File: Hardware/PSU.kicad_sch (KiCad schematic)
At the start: 0 parts

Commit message: started regulator circuit, EN circuit is not finished yet
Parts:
- added BT1, BT2, BT3: Battery_Cell, symbol Device:Battery_Cell
- added C14, C15, C16, C17, C18, C19: C, symbol Device:C
- added R12, R13, R14, R15: R, symbol Device:R
- added SW1: SW_SPDT, symbol Switch:SW_SPDT
- added U4: TLV74115_SOT23-5, Package_TO_SOT_SMD:SOT-23-5, symbol Custom_Regulator_Linear:TLV74115_SOT23-5
- added U5: TLV74133_SOT23-5, Package_TO_SOT_SMD:SOT-23-5, symbol Custom_Regulator_Linear:TLV74133_SOT23-5
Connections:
- new net: C18.1, R12.1, R13.2, U5.3 (EN)
- new net: C14.1, U5.1 (IN)
- new net: C16.1, U4.1 (IN)
- new net: C19.1, R14.2, R15.1, U4.3 (EN)
- new net +BATT: BT3.1 (+), SW1.2 (B)
- new net 1V5: C17.1, U4.5 (OUT)
- new net 3V3: C15.1, U5.5 (OUT)
- new net C1: BT1.1 (+), BT2.2 (-)
- new net C2: BT2.1 (+), BT3.2 (-)
- new net GND: BT1.2 (-), C14.2, C15.2, C16.2, C17.2, C18.2, C19.2, R12.2, R15.2, U4.2 (GND), U5.2 (GND)
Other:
- note added: "EN>=0.9V ACTIVE EN<=0.4V INACTIVE 3.9V/0.4V9.75V/V 3.9V/10V/V=0.39V"
- note added: "VBATT_MAX_ALKALINE=3*1.6V=4.8V VBATT_MIN_ALKALINE=3*1.1V=3.3V V_DROPOUT_MAX=540mV@150mA 3.3V+540mV≈3.9V"

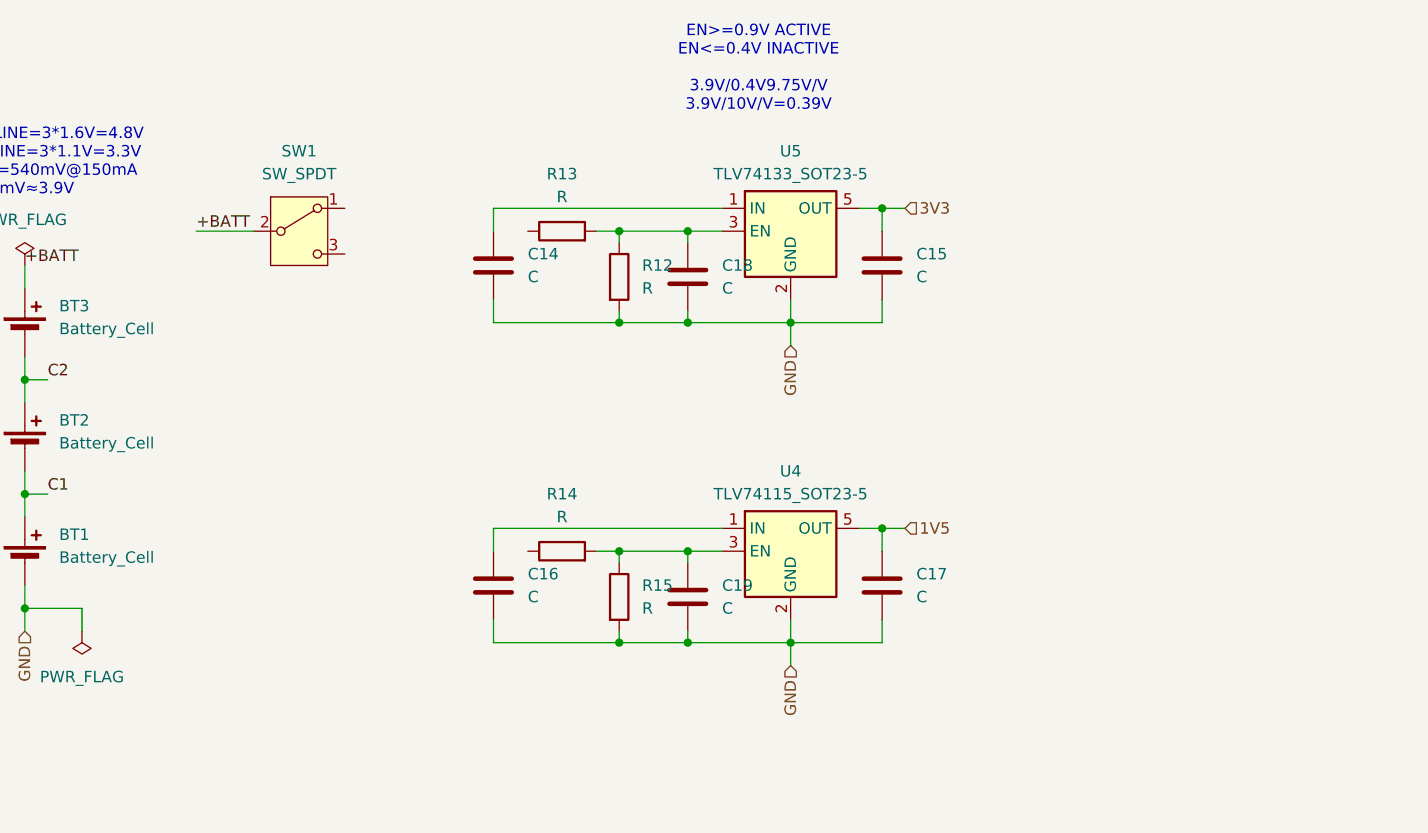
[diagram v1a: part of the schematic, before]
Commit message: Did to much for one commit BAD
- calculated values for EN divider in PSU sheet
- added power flag to switch output in PSU sheet
- connected the different sheets in the Root page
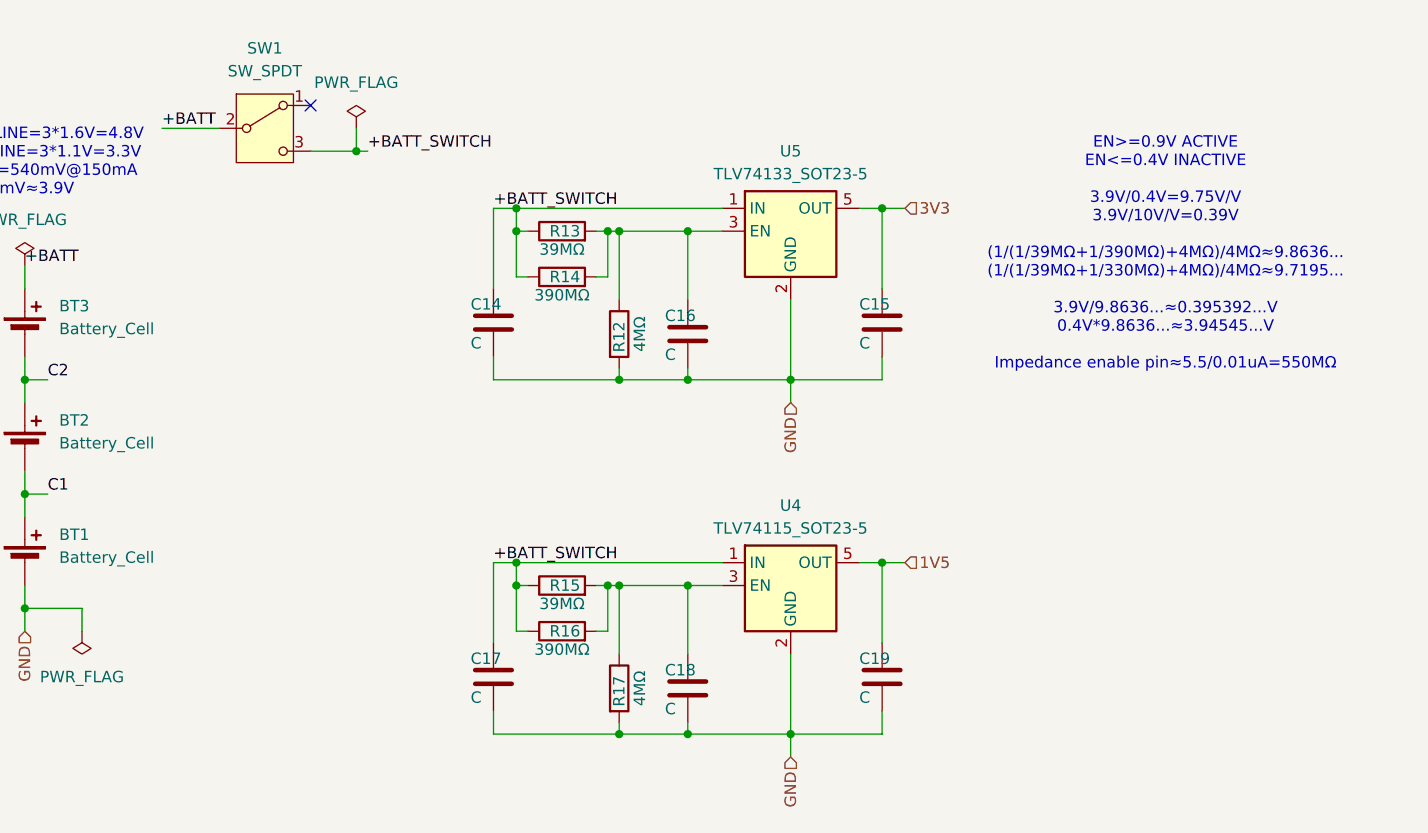
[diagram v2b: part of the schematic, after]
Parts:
- added R16: 390MΩ, symbol Device:R
- added R17: 4MΩ, symbol Device:R
- R12: value R -> 4MΩ
- R13, R15: value R -> 39MΩ
- R14: value R -> 390MΩ
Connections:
- net 1V5: now also C19.1; no longer C17.1
- net GND: now also R17.2; no longer R15.2
- net +BATT_SWITCH: now reaches R13.1
- net +BATT_SWITCH: now also C14.1, C17.1, R14.1, R15.1, SW1.3 (C), U4.1 (IN), U5.1 (IN), R16.1
- net at R12.1, R13.2, U5.3 (EN): now also C16.1, R14.2; no longer C18.1
- new net: C18.1, R15.2, R16.2, R17.1, U4.3 (EN)
- no-connect marks 0 -> 1
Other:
- note added: "EN>=0.9V ACTIVE EN<=0.4V INACTIVE 3.9V/0.4V=9.75V/V 3.9V/10V/V=0.39V (1/(1/39MΩ+1/390MΩ)+4MΩ)/4MΩ≈9.8636... (1/(1/39MΩ+1/330MΩ)+4MΩ)/4MΩ≈9.7195... 3.9V/9.8636...≈0.395392...V 0.4V*9.8636...≈3.94545...V Impedance enable pin≈5.5/0.01uA=550MΩ"
- note removed: "EN>=0.9V ACTIVE EN<=0.4V INACTIVE 3.9V/0.4V9.75V/V 3.9V/10V/V=0.39V"
- moved on the sheet: SW1

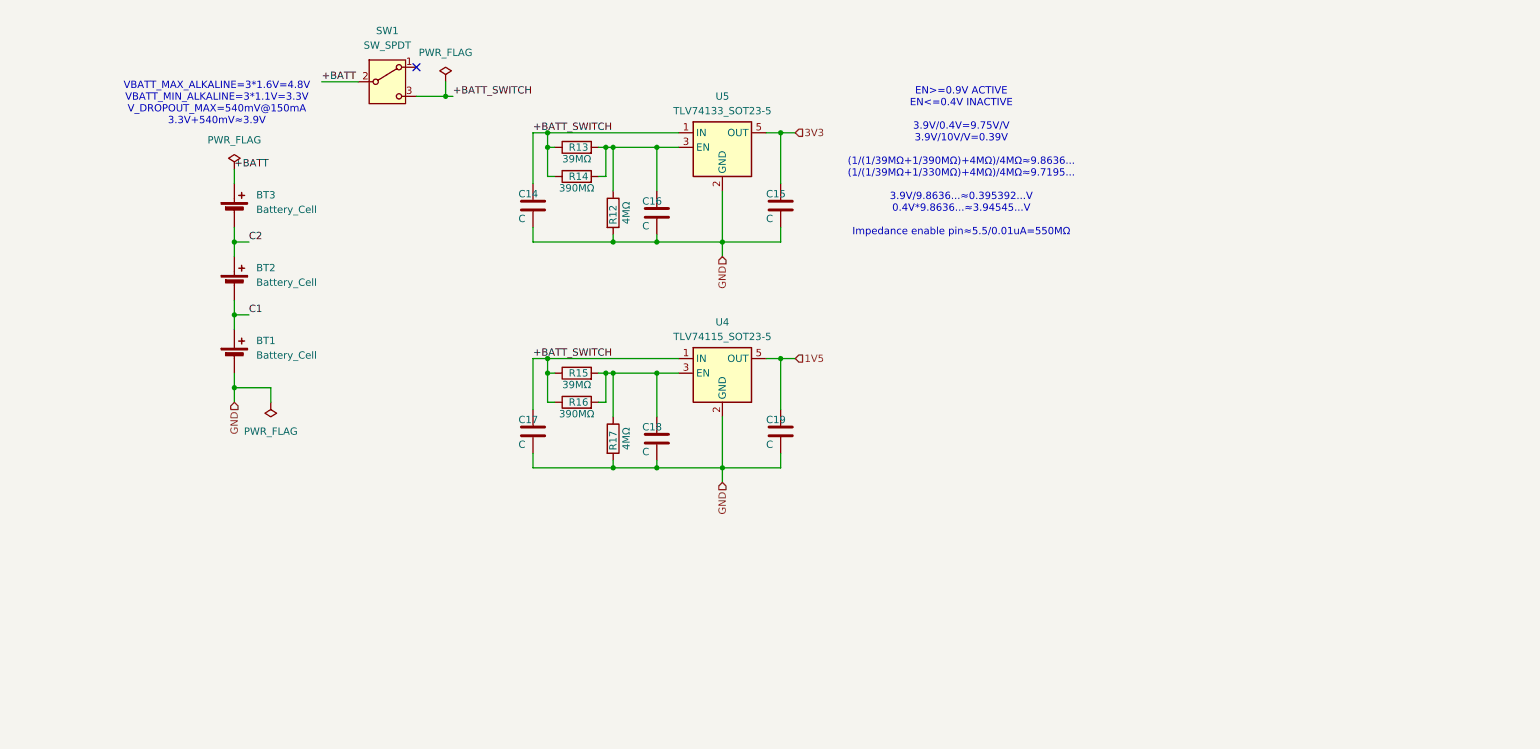
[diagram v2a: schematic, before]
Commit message: added power led to 3V3 and explained why it's not possible for 1V5 with a simple circuit
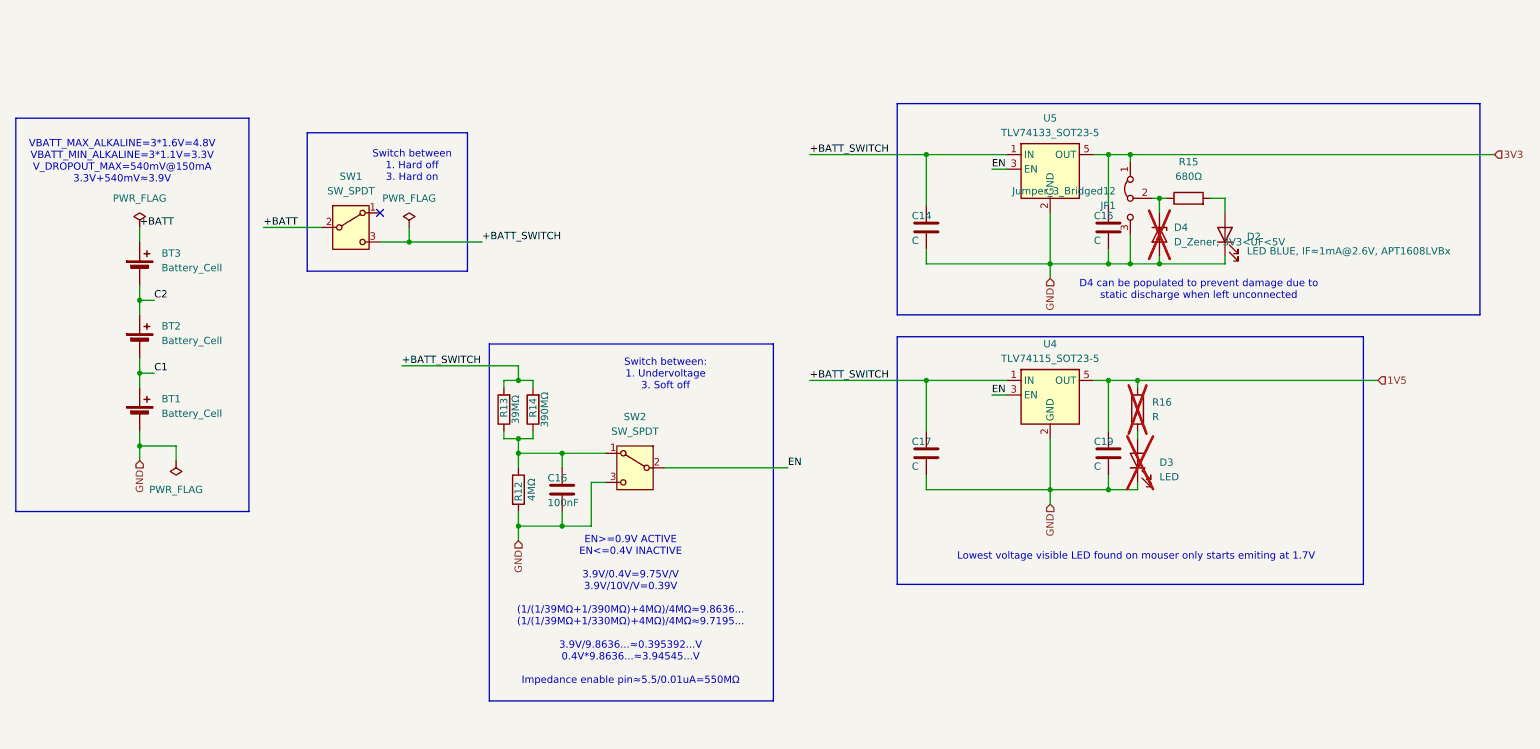
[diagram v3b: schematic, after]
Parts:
- removed C18: C, symbol Device:C
- removed R17: 4MΩ, symbol Device:R
- added D2: LED BLUE, IF≈1mA@2.6V, APT1608LVBx, symbol Device:LED
- added D3: LED, symbol Device:LED
- added D4: D_Zener, 3V3<UF<5V, symbol Device:D_Zener
- added JP1: Jumper_3_Bridged12, symbol Jumper:Jumper_3_Bridged12
- added SW2: SW_SPDT, symbol Switch:SW_SPDT
- C16: value C -> 100nF
- R15: value 39MΩ -> 680Ω
- R16: value 390MΩ -> R; now not fitted
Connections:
- net +BATT_SWITCH: now also R13.2, R14.2; no longer R13.1, R14.1, R15.1, R16.1
- net 1V5: now also R16.1
- net 3V3: now also JP1.1 (A)
- net GND: now also D2.1 (K), D3.1 (K), D4.2 (A), JP1.3 (B), SW2.3 (C)
- new net: D3.2 (A), R16.2
- new net: D2.2 (A), R15.2
- new net: C16.1, R12.1, R13.1, R14.1, SW2.1 (A)
- new net: D4.1 (K), JP1.2 (C), R15.1
- new net EN: SW2.2 (B), U4.3 (EN), U5.3 (EN)
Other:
- note added: "D4 can be populated to prevent damage due to static discharge when left unconnected"
- note added: "Lowest voltage visible LED found on mouser only starts emiting at 1.7V"
- note added: "Switch between 1. Hard off 3. Hard on"
- note added: "Switch between: 1. Undervoltage 3. Soft off"
- moved on the sheet: BT1, BT2, BT3, C14, C15, C16, C17, C19, R12, R13, R14, SW1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

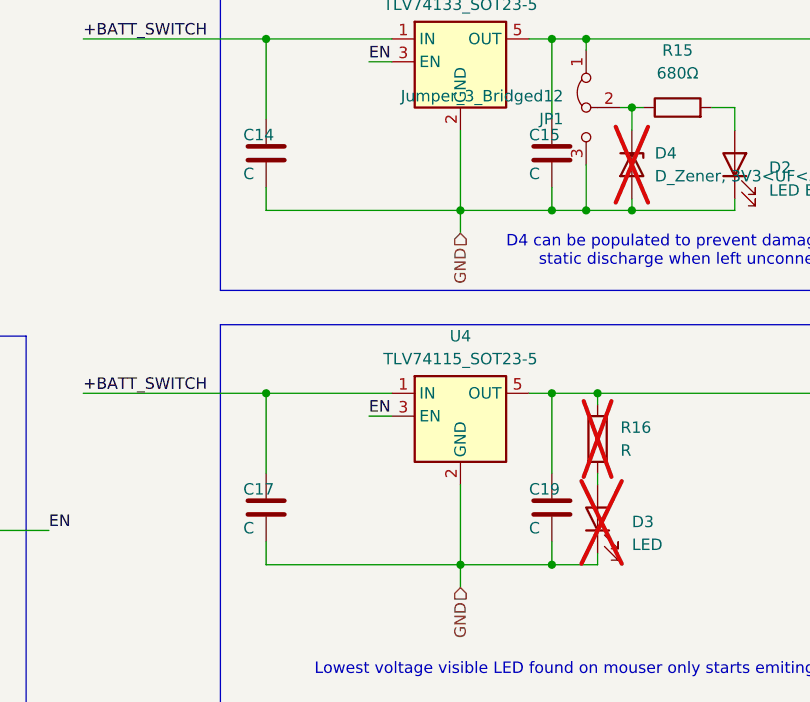
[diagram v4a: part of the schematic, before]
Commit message: Started linking footprints and work on the pcb layout
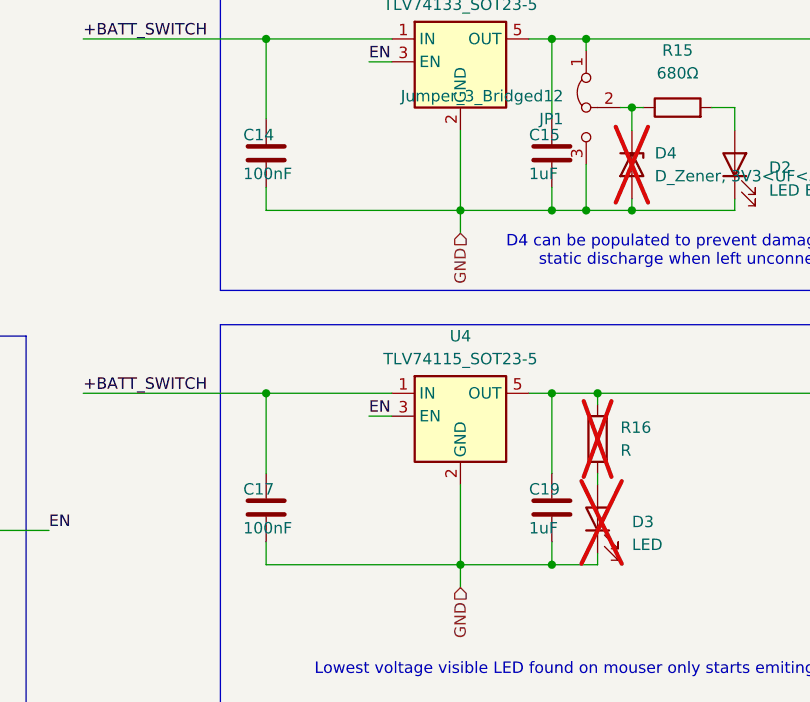
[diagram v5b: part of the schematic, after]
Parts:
- C14, C17: value C -> 100nF; footprint (none) -> Capacitor_SMD:C_0402_1005Metric_Pad0.74x0.62mm_HandSolder
- C15, C19: value C -> 1uF; footprint (none) -> Capacitor_SMD:C_0603_1608Metric_Pad1.08x0.95mm_HandSolder
- C16: footprint (none) -> Capacitor_SMD:C_0402_1005Metric_Pad0.74x0.62mm_HandSolder
- D3, R16: now left out of the parts list
- JP1: footprint (none) -> Jumper:SolderJumper-3_P1.3mm_Bridged2Bar12_Pad1.0x1.5mm
- R15: footprint (none) -> Resistor_SMD:R_0402_1005Metric_Pad0.72x0.64mm_HandSolder
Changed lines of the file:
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@@
 			)
 		)
-		(property "Value" "C"
+		(property "Value" "100nF"
 			(at 173.99 53.086 0)
 			(effects
@@
 			)
 		)
-		(property "Footprint" ""
+		(property "Footprint" "Capacitor_SMD:C_0402_1005Metric_Pad0.74x0.62mm_HandSolder"
 			(at 177.4952 54.61 0)
 			(effects
@@
 		(unit 1)
 		(exclude_from_sim no)
-		(in_bom yes)
-		(on_board yes)
+		(in_bom no)
+		(on_board no)
 		(dnp yes)
 		(fields_autoplaced yes)
@@
 			)
 		)
-		(property "Value" "C"
+		(property "Value" "1uF"
 			(at 205.74 92.456 0)
 			(effects
@@
 			)
 		)
-		(property "Footprint" ""
+		(property "Footprint" "Capacitor_SMD:C_0603_1608Metric_Pad1.08x0.95mm_HandSolder"
 			(at 209.2452 93.98 0)
 			(effects
@@
 			)
 		)
-		(property "Footprint" ""
+		(property "Footprint" "Jumper:SolderJumper-3_P1.3mm_Bridged2Bar12_Pad1.0x1.5mm"
 			(at 212.09 45.72 0)
 			(effects
@@
 			)
 		)
-		(property "Value" "C"
+		(property "Value" "100nF"
 			(at 173.99 92.456 0)
 			(effects
@@
 			)
 		)
-		(property "Footprint" ""
+		(property "Footprint" "Capacitor_SMD:C_0402_1005Metric_Pad0.74x0.62mm_HandSolder"
 			(at 177.4952 93.98 0)
 			(effects
@@
 			)
 		)
-		(property "Footprint" ""
+		(property "Footprint" "Capacitor_SMD:C_0402_1005Metric_Pad0.74x0.62mm_HandSolder"
 			(at 113.9952 100.33 0)
 			(effects
@@
 			)
 		)
-		(property "Value" "C"
+		(property "Value" "1uF"
 			(at 205.74 53.086 0)
 			(effects
@@
 			)
 		)
-		(property "Footprint" ""
+		(property "Footprint" "Capacitor_SMD:C_0603_1608Metric_Pad1.08x0.95mm_HandSolder"
 			(at 209.2452 54.61 0)
 			(effects
@@
 			)
 		)
-		(property "Footprint" ""
+		(property "Footprint" "Resistor_SMD:R_0402_1005Metric_Pad0.72x0.64mm_HandSolder"
 			(at 222.25 47.498 90)
 			(effects
@@
 		(unit 1)
 		(exclude_from_sim no)
-		(in_bom yes)
-		(on_board yes)
+		(in_bom no)
+		(on_board no)
 		(dnp yes)
 		(fields_autoplaced yes)
